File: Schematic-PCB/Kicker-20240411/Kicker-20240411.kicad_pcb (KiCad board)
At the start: 2 copper layers, 90.8 x 64.3 mm, 23 parts, among them J1 Conn_01x02_Pin, J2 Conn_01x05_Pin, J3 Conn_01x02_Pin, Q1 NMOS, Q2 NMOS, U1 TSSP58P38, U2 TSSP58P38

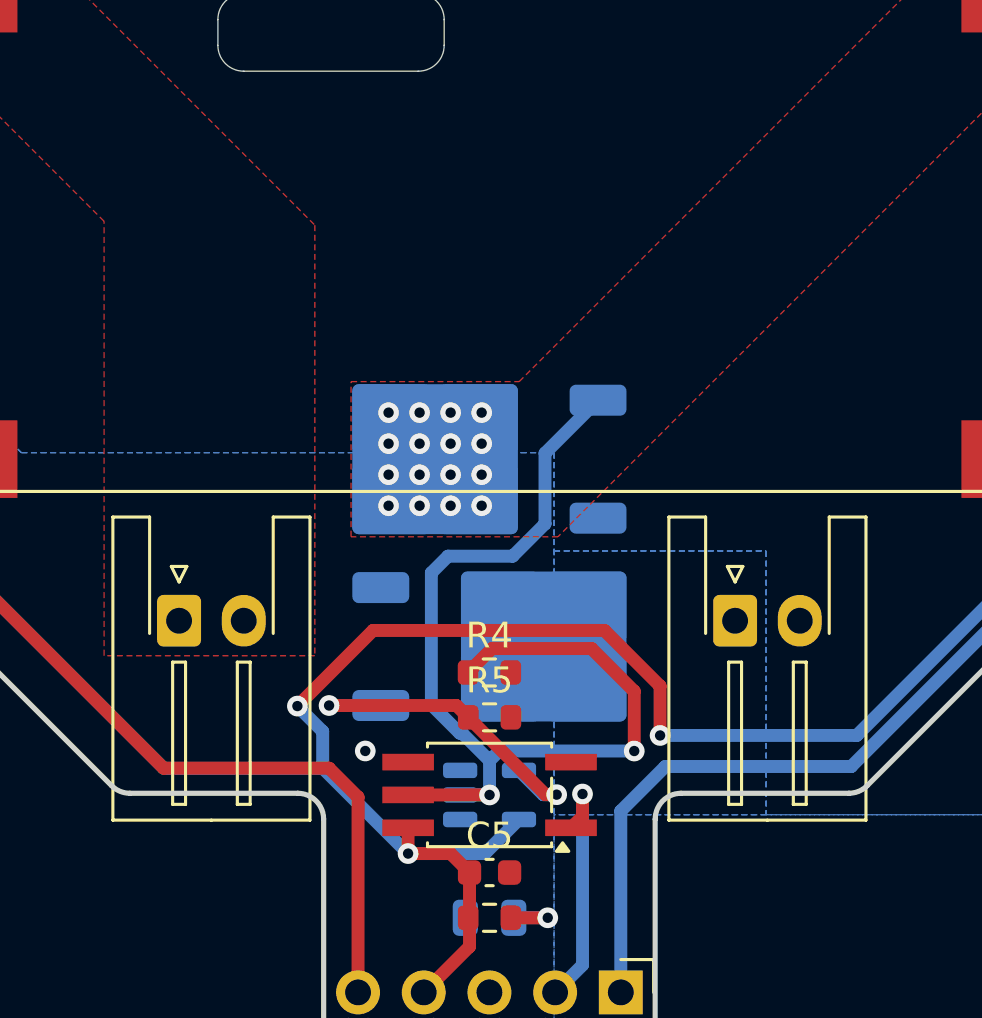
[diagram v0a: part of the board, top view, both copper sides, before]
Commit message: キッカー基板にロゴとか入れるの忘れてたのを追加した
JLCPCBロゴとチームロゴ、キッカー基板のバージョン
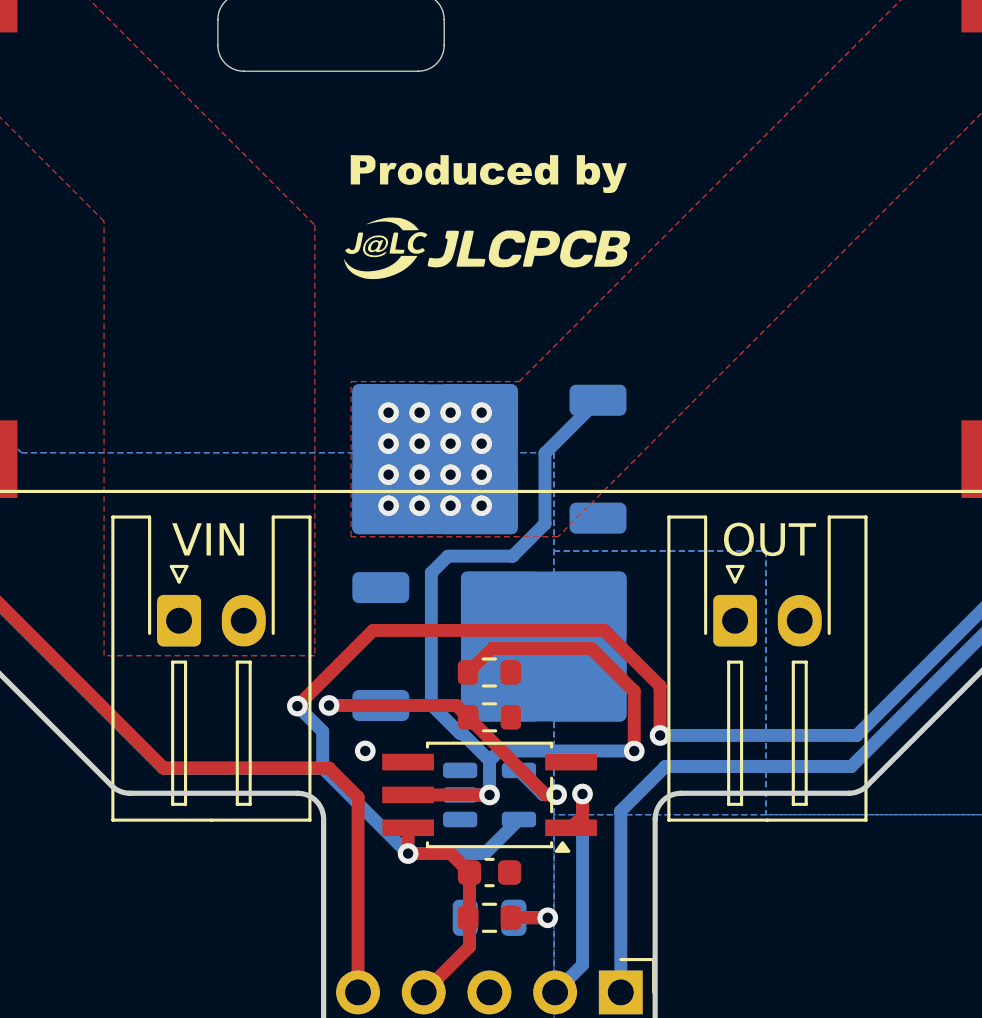
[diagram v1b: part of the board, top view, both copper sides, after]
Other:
- board text added: "Kicker-Board #003"
- board text added: "OUT"
- board text added: "PWR"
- board text added: "VIN"

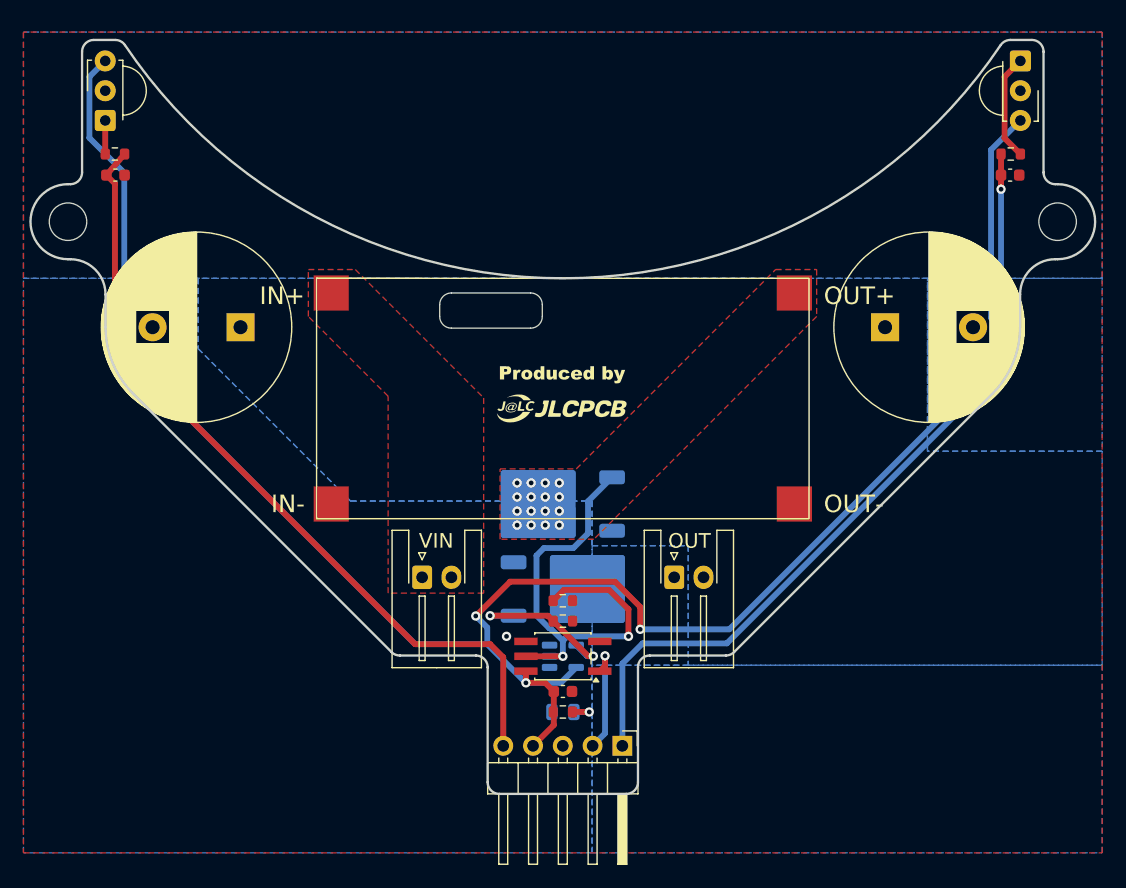
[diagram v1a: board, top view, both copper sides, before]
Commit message: キッカー基板更新した
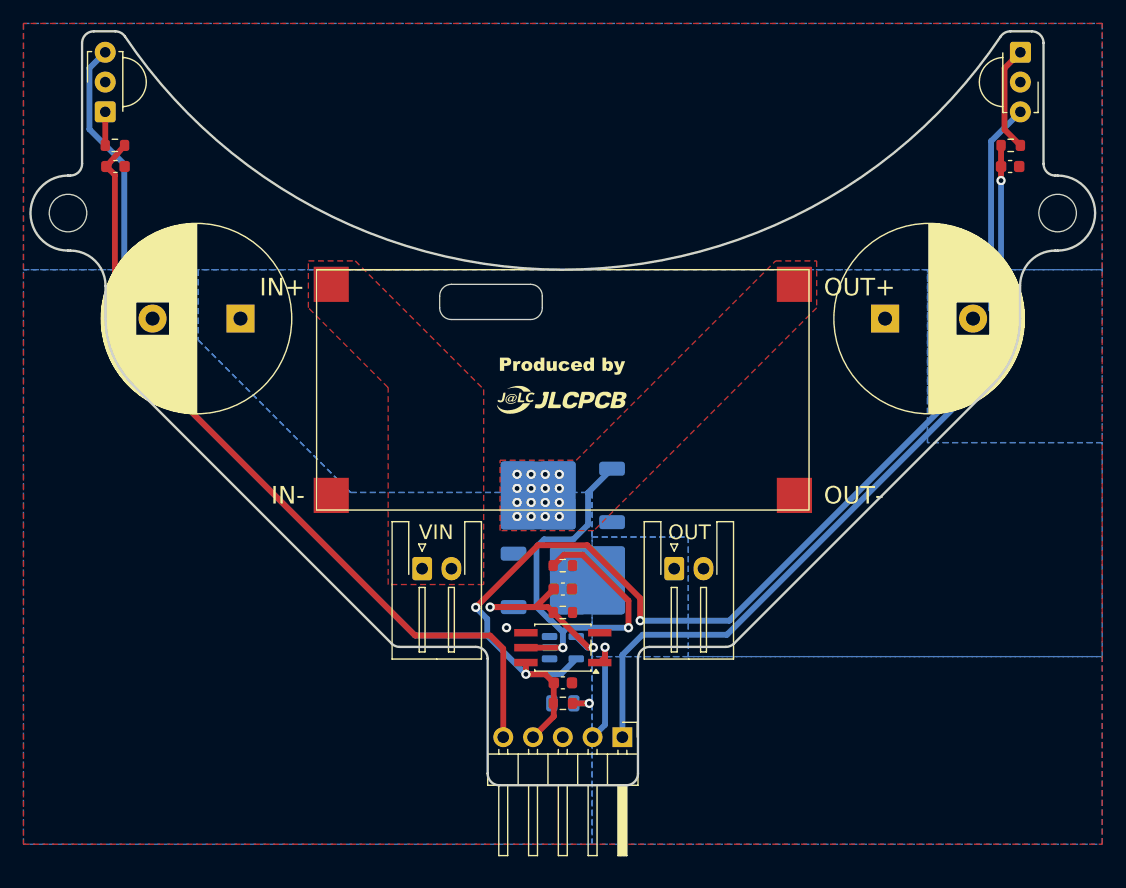
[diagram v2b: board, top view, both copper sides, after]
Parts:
- added C7: 0.1uF, Capacitor_SMD:C_0603_1608Metric, F.Cu at (0.00, 26.5)
- moved R4 3.00 mm to (0.00, 24.5)
- moved C5 0.74 mm to (0.01, 34.5)
- moved D1 0.74 mm to (0.01, 36.2)
- moved D2 0.74 mm to (0.01, 31.5)
- moved J1 0.74 mm to (-12.0, 24.8)
- moved J2 0.74 mm to (5.08, 39.1)
- moved J3 0.74 mm to (9.50, 24.8)
- moved Q1 0.74 mm to (-0.84, 18.5)
- moved R3 0.74 mm to (0.01, 36.2)
- moved R5 0.74 mm to (0.01, 28.5)
- moved U1 0.74 mm to (39.0, -19.3)
- moved U4 0.74 mm to (0.01, 31.5)
- moved REF** 0.74 mm to (-42.2, -5.56)
- moved REF** 0.74 mm to (42.2, -5.56)
- moved C1 0.74 mm to (27.5, 3.44)
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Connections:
- Q1 pad 3: VDD -> Net-(D3-K)
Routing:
- net Net-(Q2-G): track 14.1 -> 20.1 mm
- net +3.3V: track 168.7 -> 170.7 mm
- net Sig: track 40.2 -> 41.2 mm

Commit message: コミット。
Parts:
- added VIN: Conn_01x02_Pin, Connector_JST:JST_XH_S2B-XH-A-1_1x02_P2.50mm_Horizontal, F.Cu at (182.5, 121.7)
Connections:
- C1 pad 1: VDD -> VCC

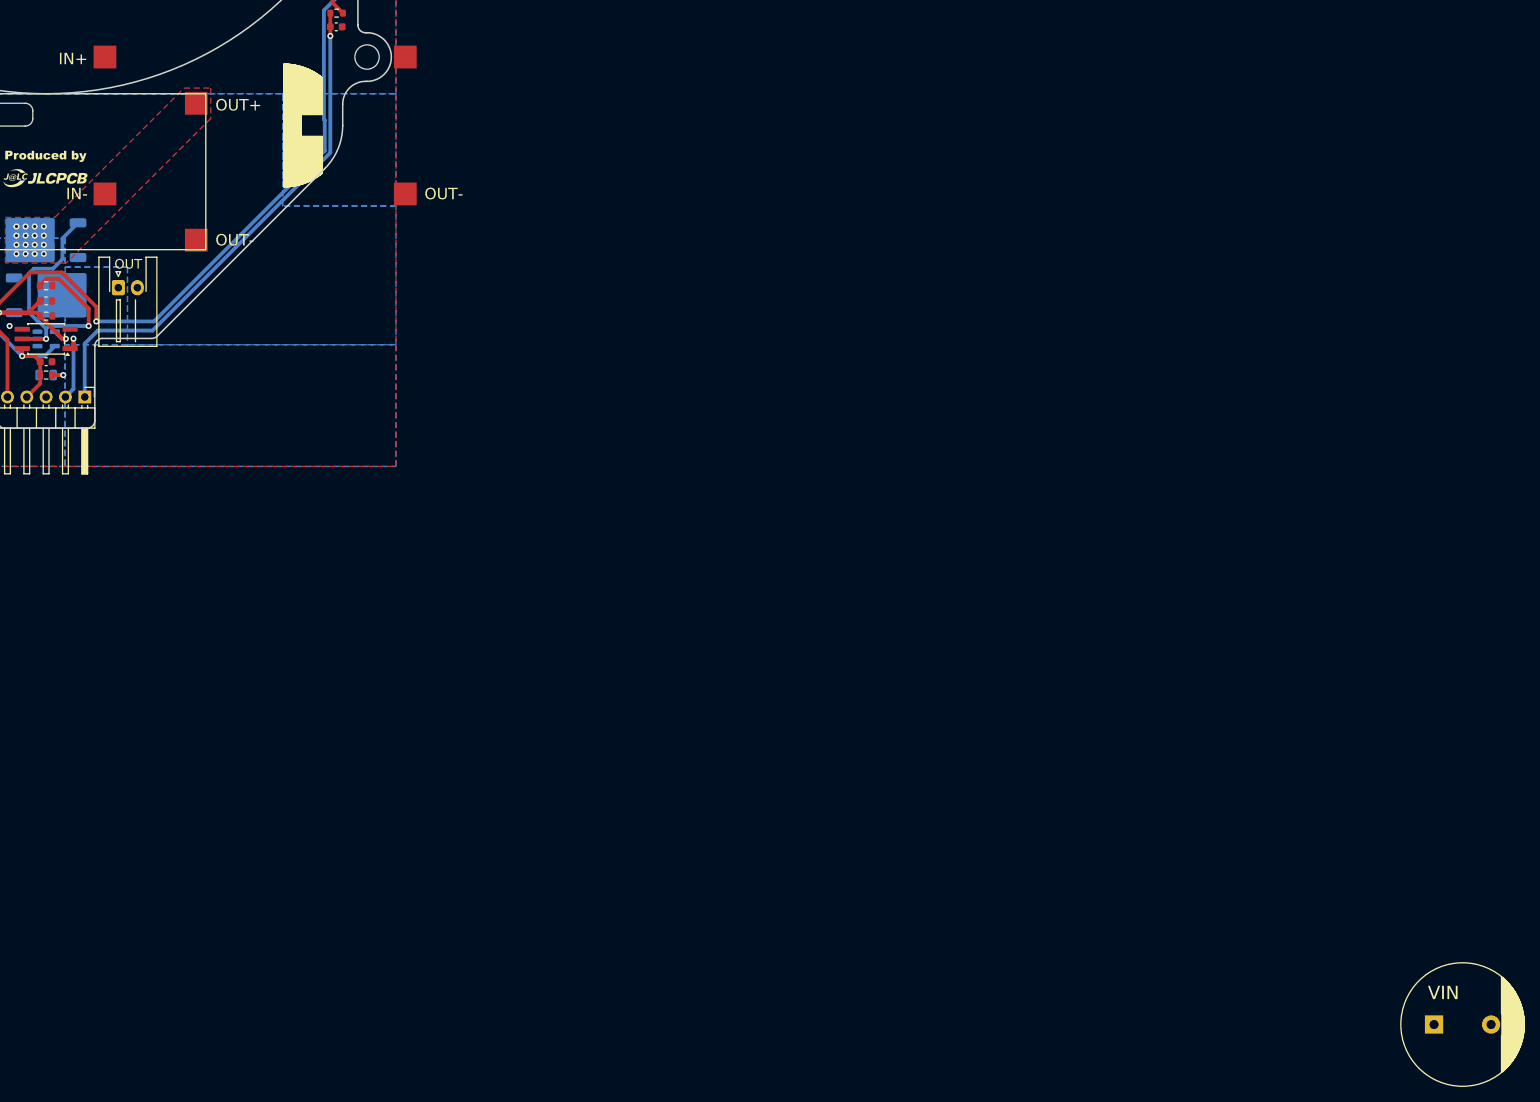
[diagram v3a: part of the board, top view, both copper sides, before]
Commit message: キッカー基板が開けないのを解消した
進捗生んだ。
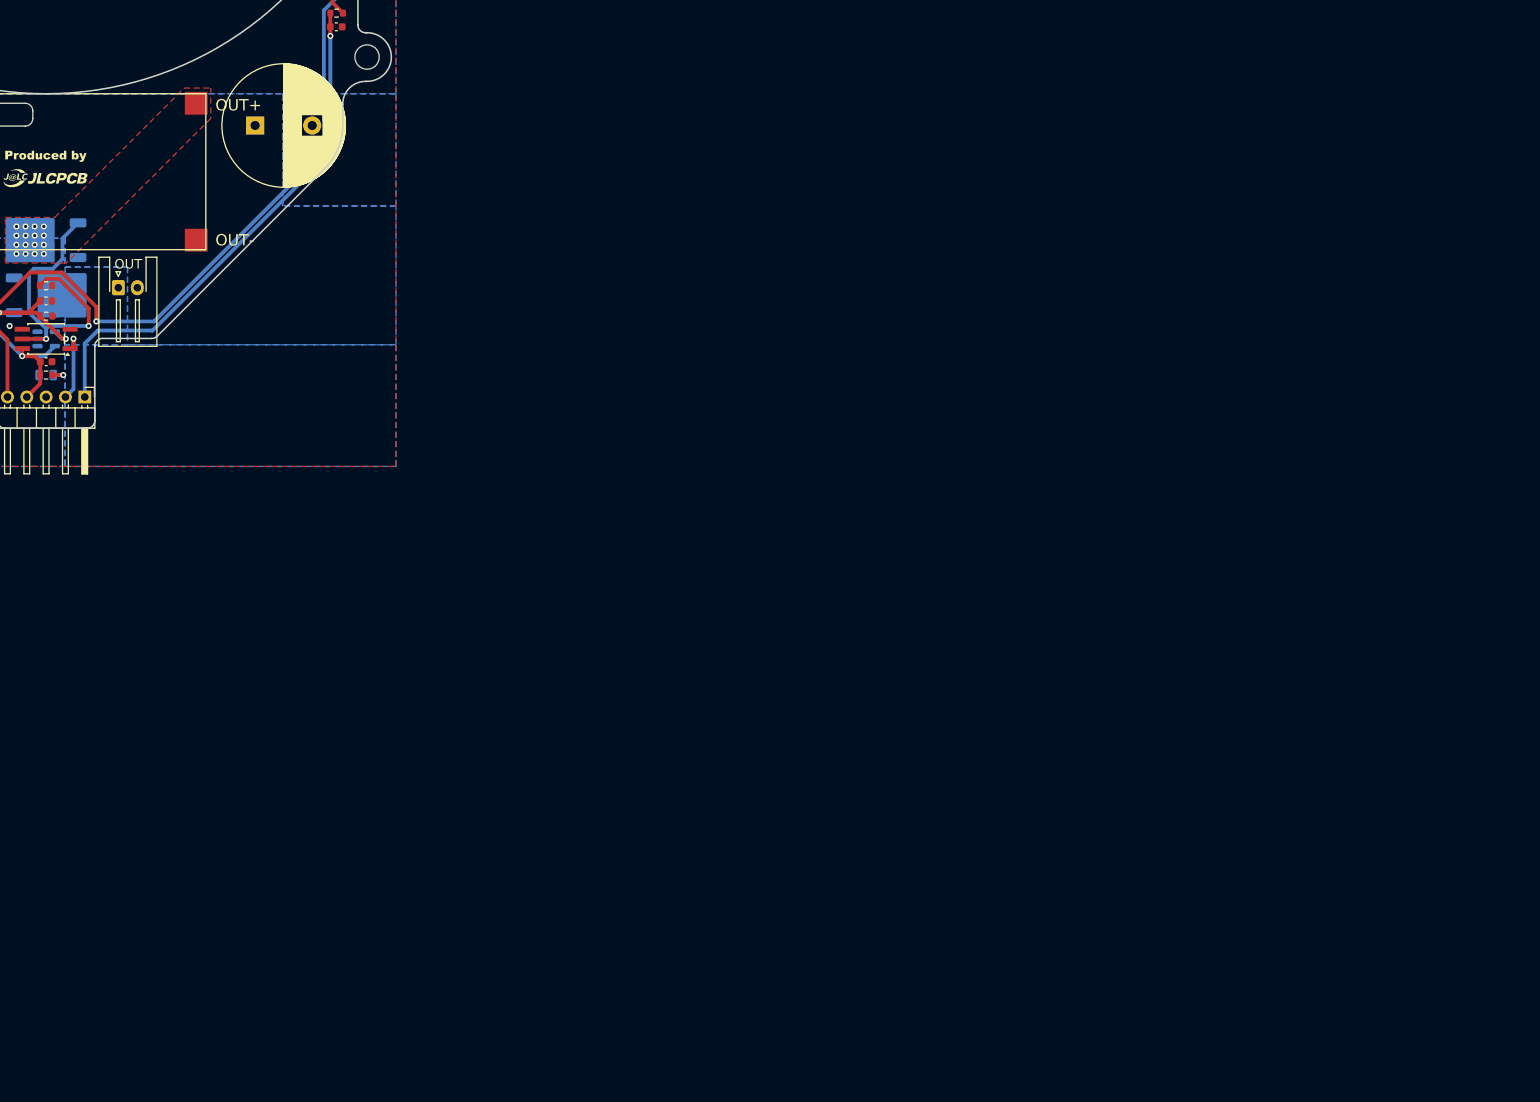
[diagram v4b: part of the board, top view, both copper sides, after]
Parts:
- removed VIN: Conn_01x02_Pin, Connector_JST:JST_XH_S2B-XH-A-1_1x02_P2.50mm_Horizontal
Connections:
- C1 pad 1: VCC -> VDD

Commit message: update: キッカー基板の回路図を修正した
ツェナーダイオードをなくした
+48V-+VDD関連のNchMOSFETのロジックを削除した
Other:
- board text added: "Kicker-Board #004"
- board text removed: "Kicker-Board #003"
